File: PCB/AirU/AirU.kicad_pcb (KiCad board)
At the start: 2 copper layers, 11 parts, among them IC1 LD1086DT50TR, IC2 L70B-M39, IC3 NCV21872DR2G, J1 MEM2051-00-195-00-A, J2 ZX62-B-5PA_33_, J3 53261-7008, Q1 MMBT3904, Q2 MMBT3904, U1 ESP32-S3-WROOM-1, U2 CH340E

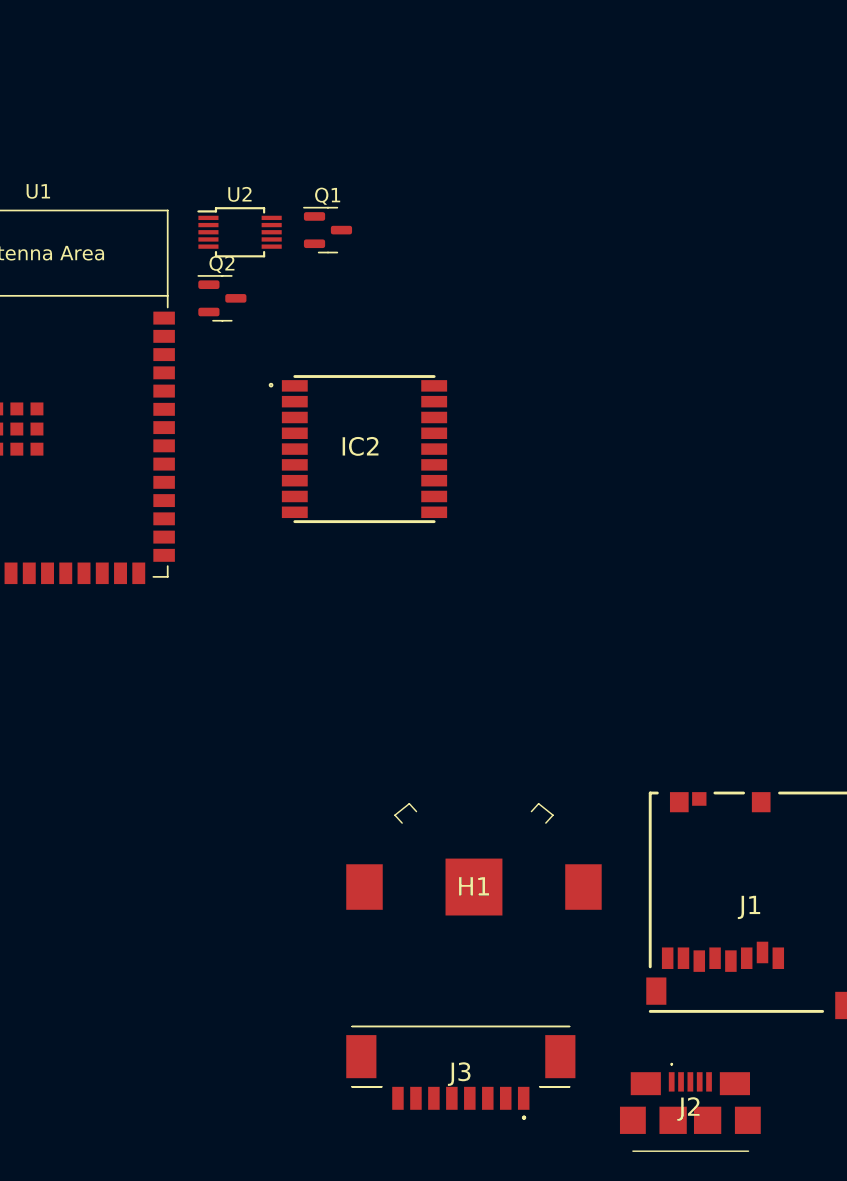
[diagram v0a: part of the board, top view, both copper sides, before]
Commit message: usb to serial done on schematic
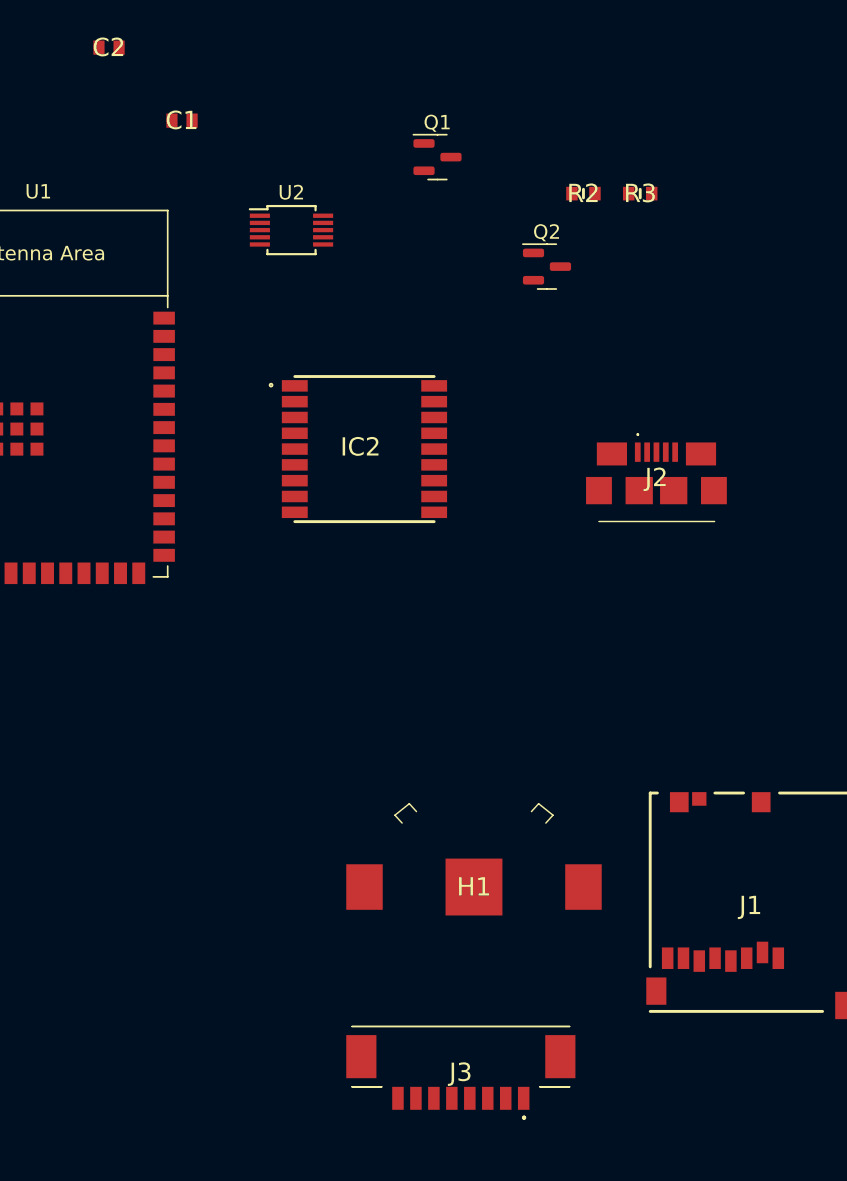
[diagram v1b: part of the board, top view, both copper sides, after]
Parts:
- added C1: 100n, 0603YC104J4T4A:CAPC1608X90N, F.Cu at (78.7, 35.6)
- added C2: 0603YC104J4T4A, 0603YC104J4T4A:CAPC1608X90N, F.Cu at (73.7, 30.5)
- added R2: RC0603FR-0710KL, RC0603FR-0710KL:RESC1608X55N, F.Cu at (106.7, 40.6)
- added R3: RC0603FR-0710KL, RC0603FR-0710KL:RESC1608X55N, F.Cu at (110.6, 40.6)
- moved J2 43.9 mm to (111.8, 61.0)
- moved Q2 22.7 mm to (104.1, 45.7)
- moved Q1 9.16 mm to (96.5, 38.1)
- moved U2 3.58 mm to (86.4, 43.2)
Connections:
- Q1 pad 1: unconnected-(Q1-Pad1) -> Net-(Q1-Pad1)
- Q1 pad 2: unconnected-(Q1-Pad2) -> Net-(Q1-Pad2)
- Q2 pad 1: unconnected-(Q2-Pad1) -> Net-(Q2-Pad1)
- Q2 pad 2: unconnected-(Q2-Pad2) -> Net-(Q2-Pad2)
- U2 pad 4: unconnected-(U2-Pad4) -> GND
- U2 pad 5: unconnected-(U2-Pad5) -> GND
- U2 pad 8: unconnected-(U2-Pad8) -> /U0RXD
- U2 pad 9: unconnected-(U2-Pad9) -> /U0TXD

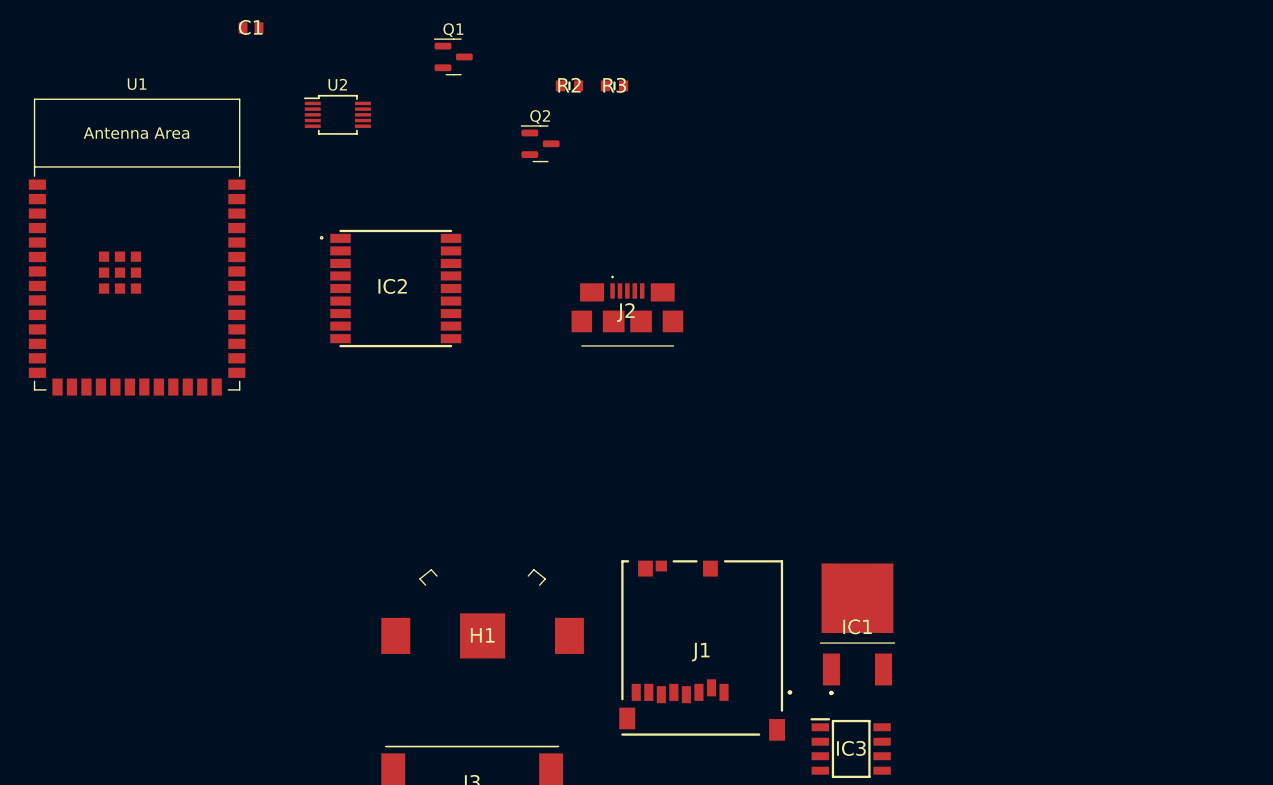
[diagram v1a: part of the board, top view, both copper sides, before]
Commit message: added footprint for lora breakout board
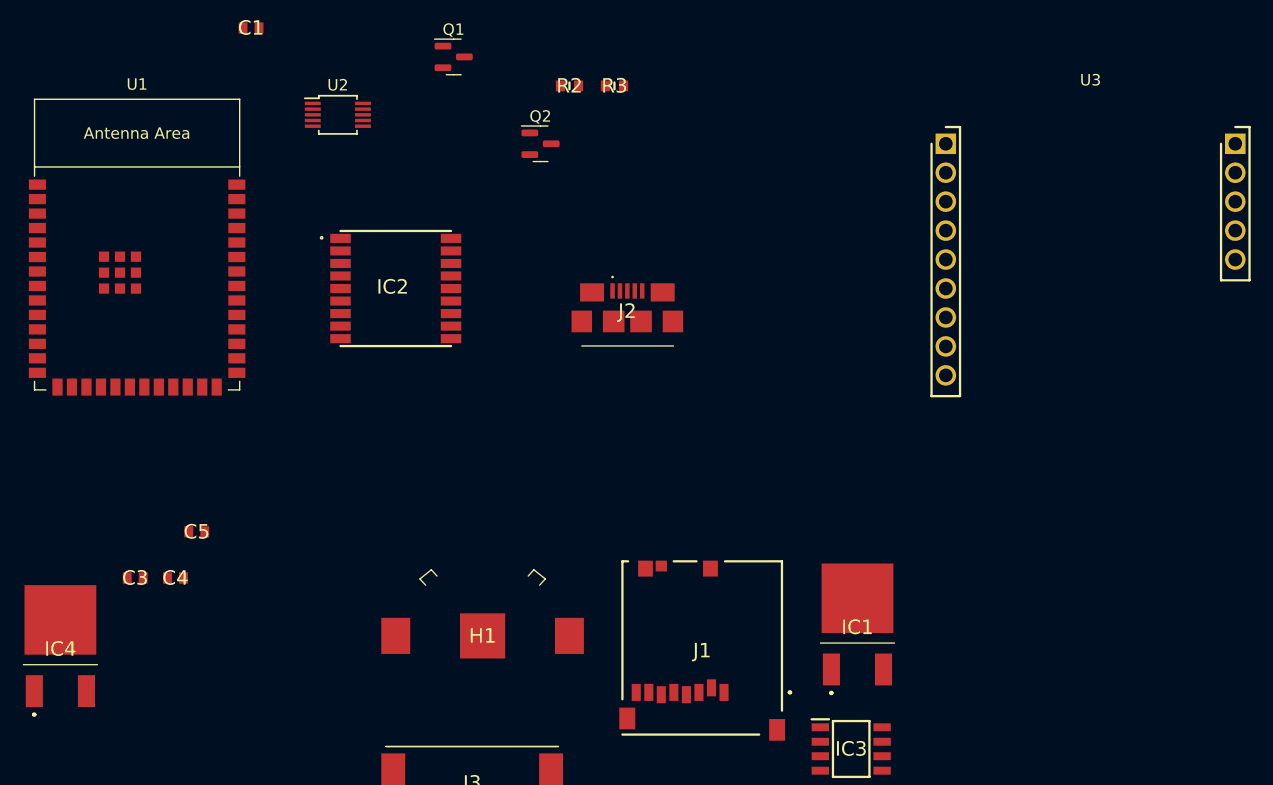
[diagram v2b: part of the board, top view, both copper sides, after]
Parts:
- added C3: 1u, 0603YC105KAT2A:CAPC1608X94N, F.Cu at (68.6, 83.8)
- added C4: 10u, 0603ZDD106KAT2A:CAPC1608X90N, F.Cu at (72.1, 83.8)
- added C5: 10u, 0603ZDD106KAT2A:CAPC1608X90N, F.Cu at (74.0, 79.8)
- added IC4: LD1086DT50TR, LD1086DT50TR:LD1086DT33TR, F.Cu at (62.0, 84.4)
- added U3: LoRa_Breakout, custom_components:LoRa_Breakout, F.Cu at (152.4, 40.6)
- C1: value 100n -> 0.1u
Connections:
- J2 pad 1: unconnected-(J2-Pad1) -> VCC
- J2 pad 2: unconnected-(J2-Pad2) -> /D-
- J2 pad 3: unconnected-(J2-Pad3) -> /D+
- J2 pad 5: unconnected-(J2-Pad5) -> GND
- J2 pad MP1: unconnected-(J2-PadMP1) -> GND
- J2 pad MP2: unconnected-(J2-PadMP2) -> GND
- J2 pad MP3: unconnected-(J2-PadMP3) -> GND
- J2 pad MP4: unconnected-(J2-PadMP4) -> GND
- J2 pad MP5: unconnected-(J2-PadMP5) -> GND
- J2 pad MP6: unconnected-(J2-PadMP6) -> GND
- U1 pad 3: /EN -> VDD

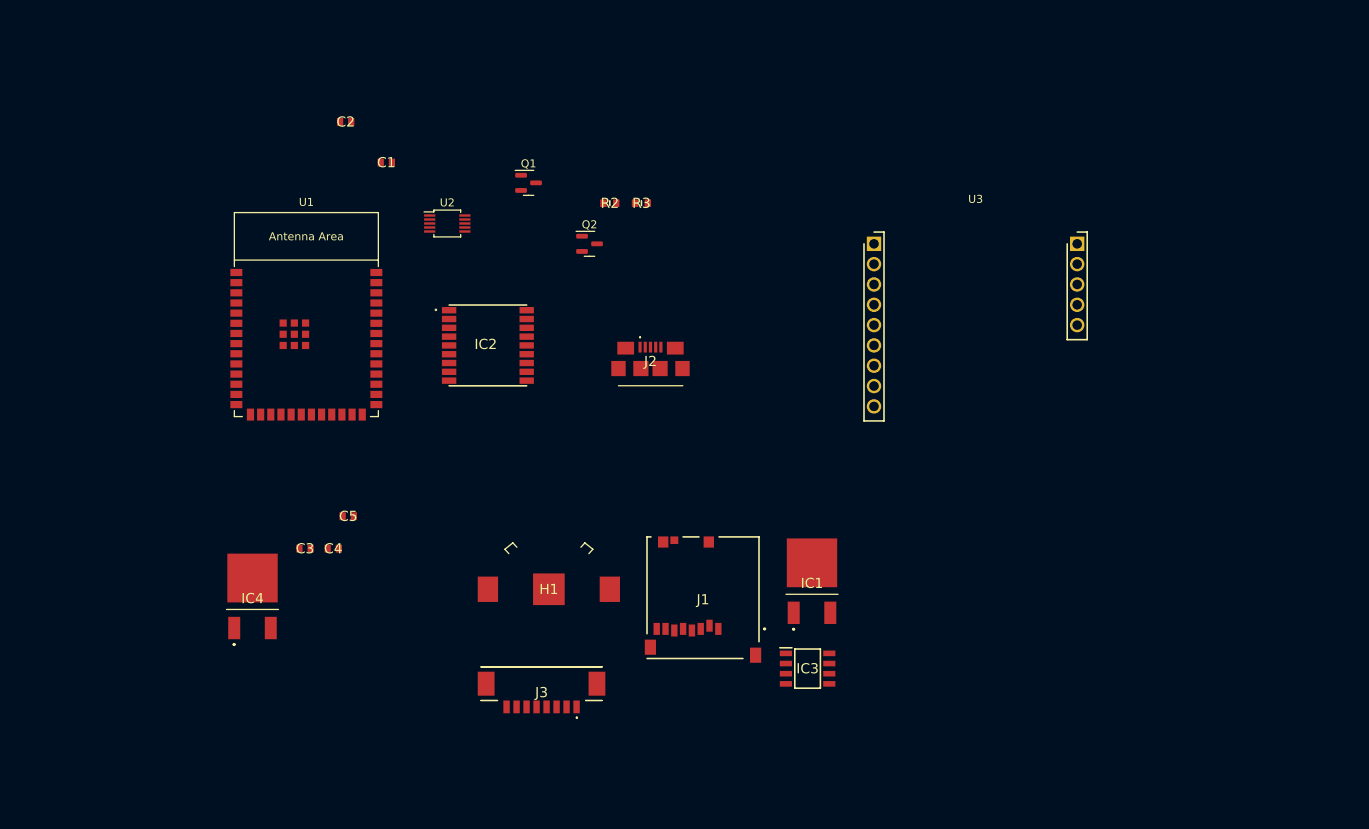
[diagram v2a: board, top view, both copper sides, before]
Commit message: added most parts to pcb
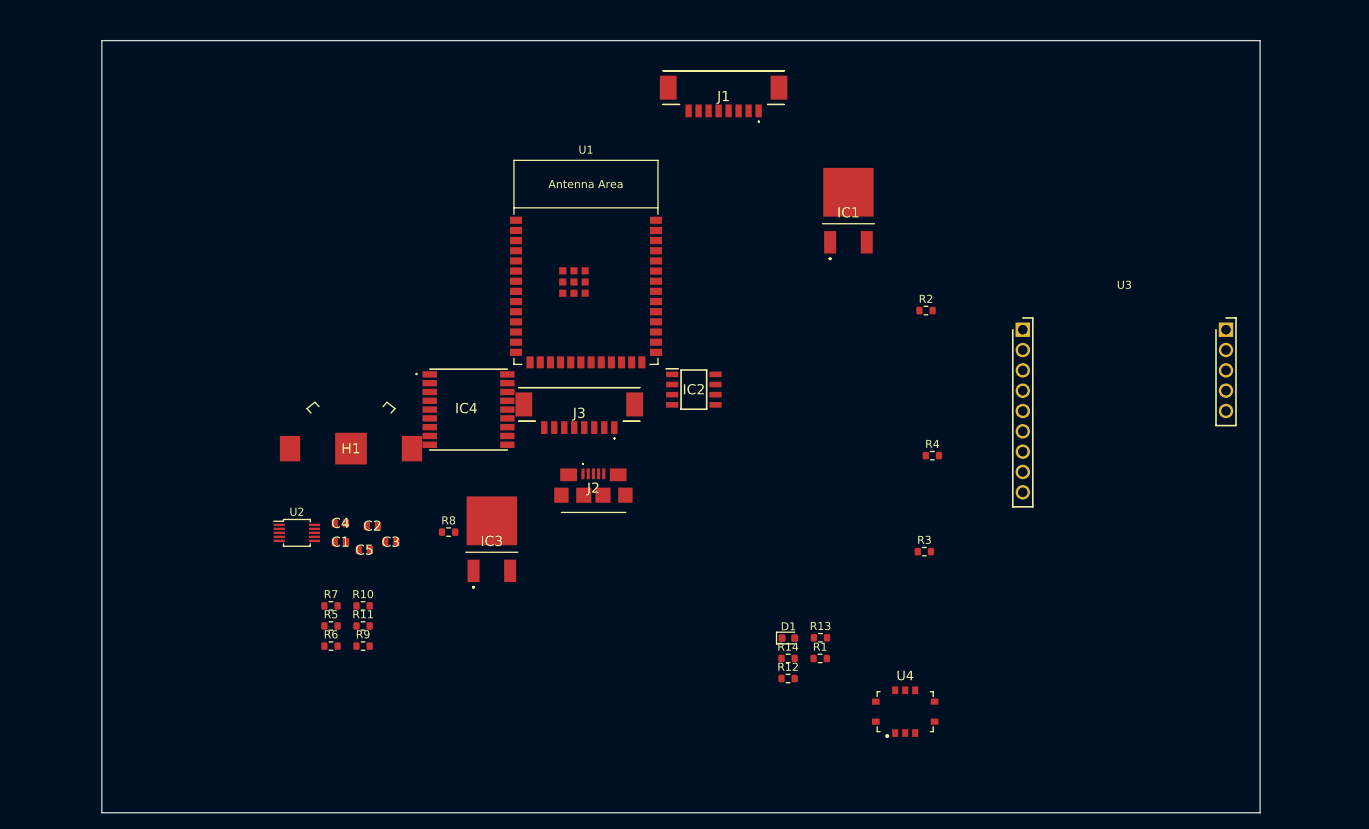
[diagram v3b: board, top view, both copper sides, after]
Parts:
- removed Q1, Q2: MMBT3904, Package_TO_SOT_SMD:SOT-23
- added D1: LED, LED_SMD:LED_0603_1608Metric, F.Cu at (129.0, 95.0)
- added R1: 0, Resistor_SMD:R_0603_1608Metric, F.Cu at (133.0, 97.5)
- added R10: 0, Resistor_SMD:R_0603_1608Metric, F.Cu at (75.8, 91.0)
- added R11: 0, Resistor_SMD:R_0603_1608Metric, F.Cu at (75.8, 93.5)
- added R12: 820, Resistor_SMD:R_0603_1608Metric, F.Cu at (129.0, 100.1)
- added R13: 130, Resistor_SMD:R_0603_1608Metric, F.Cu at (133.0, 95.0)
- added R14: 27, Resistor_SMD:R_0603_1608Metric, F.Cu at (129.0, 97.5)
- added R4: 0, Resistor_SMD:R_0603_1608Metric, F.Cu at (147.0, 72.2)
- added R5: 0, Resistor_SMD:R_0603_1608Metric, F.Cu at (71.8, 93.5)
- added R6: 0, Resistor_SMD:R_0603_1608Metric, F.Cu at (71.8, 96.0)
- added R7: 0, Resistor_SMD:R_0603_1608Metric, F.Cu at (71.8, 91.0)
- added R8: 0, Resistor_SMD:R_0603_1608Metric, F.Cu at (86.5, 81.8)
- added R9: 0, Resistor_SMD:R_0603_1608Metric, F.Cu at (75.8, 96.0)
- added U4: MICS6814, chem_air_u_footprints:PLCC125P750X550X150-16N, F.Cu at (143.6, 104.2)
- C1: value 0.1u -> 0603YC105KAT2A; footprint 0603YC104J4T4A:CAPC1608X90N -> 0603YC105KAT2A:CAPC1608X94N
- C2: value 0603YC104J4T4A -> 10u; footprint 0603YC104J4T4A:CAPC1608X90N -> 0603ZDD106KAT2A:CAPC1608X90N
- C3: value 1u -> 0603YC104J4T4A; footprint 0603YC105KAT2A:CAPC1608X94N -> 0603YC104J4T4A:CAPC1608X90N
- C5: value 10u -> 0.1u; footprint 0603ZDD106KAT2A:CAPC1608X90N -> 0603YC104J4T4A:CAPC1608X90N
- IC2: value L70B-M39 -> NCV21872DR2G; footprint L70B-M39:L76 -> NCV21872DR2G:SOIC127P600X175-8N
- IC3: value NCV21872DR2G -> LD1086DT50TR; footprint NCV21872DR2G:SOIC127P600X175-8N -> LD1086DT50TR:LD1086DT33TR
- IC4: value LD1086DT50TR -> L70B-M39; footprint LD1086DT50TR:LD1086DT33TR -> L70B-M39:L76
- J1: value MEM2051-00-195-00-A -> 53261-7008; footprint MEM2051-00-195-00-A:MEM20510019500A -> 53261-7008:532617008
- R2, R3: value RC0603FR-0710KL -> 0; footprint RC0603FR-0710KL:RESC1608X55N -> Resistor_SMD:R_0603_1608Metric
- moved J1 64.0 mm to (120.9, 26.2)
- moved R3 56.1 mm to (146.0, 84.2)
- moved C2 50.6 mm to (77.0, 81.0)
- moved C1 47.8 mm to (73.0, 83.0)
- moved IC1 46.5 mm to (136.5, 36.2)
- moved IC3 45.0 mm to (91.9, 77.3)
- moved U2 43.0 mm to (67.6, 81.8)
- moved R2 41.7 mm to (146.2, 54.1)
- moved U1 35.6 mm to (103.7, 51.0)
- moved J3 35.2 mm to (102.9, 65.8)
- moved IC4 32.5 mm to (89.0, 66.4)
- moved H1 30.3 mm to (74.3, 71.3)
- moved IC2 26.3 mm to (117.2, 63.9)
- moved U3 21.5 mm to (171.0, 51.4)
- moved J2 17.4 mm to (104.6, 76.8)
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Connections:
- C1 pad 1: VDD -> GND
- C1 pad 2: GND -> VDD
- C2 pad 1: unconnected-(C2-Pad1) -> GND
- C2 pad 2: unconnected-(C2-Pad2) -> VCC
- C3 pad 1: GND -> unconnected-(C3-Pad1)
- C3 pad 2: VDD -> unconnected-(C3-Pad2)
- C4 pad 2: VCC -> VDD
- C5 pad 1: GND -> VDD
- C5 pad 2: VDD -> GND
- IC3 pad 1: unconnected-(IC3-Pad1) -> GND
- IC3 pad 2: unconnected-(IC3-Pad2) -> VDD
- IC3 pad 3: unconnected-(IC3-Pad3) -> VCC
- IC4 pad 1: GND -> unconnected-(IC4-Pad1)
- IC4 pad 2: VDD -> unconnected-(IC4-Pad2)
- IC4 pad 3: VCC -> unconnected-(IC4-Pad3)
- J1 pad MP1: unconnected-(J1-PadMP1) -> GND
- J1 pad MP2: unconnected-(J1-PadMP2) -> GND
- R2 pad 1: Net-(Q2-Pad2) -> /LORA_SCLK
- R2 pad 2: Net-(Q1-Pad1) -> /GPIO14
- R3 pad 1: Net-(Q1-Pad2) -> /LORA_MISO
- R3 pad 2: Net-(Q2-Pad1) -> /GPIO13
- U1 pad 12: /GPIO8 -> /CO_VALUE
- U2 pad 6: unconnected-(U2-Pad6) -> Net-(D1-Pad2)
- U3 pad 1: unconnected-(U3-Pad1) -> VDD
- U3 pad 10: unconnected-(U3-Pad10) -> /LORA_DIO1
- U3 pad 11: unconnected-(U3-Pad11) -> /LORA_DIO2
- U3 pad 12: unconnected-(U3-Pad12) -> /LORA_DIO3
- U3 pad 13: unconnected-(U3-Pad13) -> /LORA_DIO4
- U3 pad 14: unconnected-(U3-Pad14) -> /LORA_DIO5
- U3 pad 2: unconnected-(U3-Pad2) -> GND
- U3 pad 3: unconnected-(U3-Pad3) -> VDD
- U3 pad 4: unconnected-(U3-Pad4) -> /LORA_DIO0
- U3 pad 5: unconnected-(U3-Pad5) -> /LORA_SCLK
- U3 pad 6: unconnected-(U3-Pad6) -> /LORA_MISO
- U3 pad 7: unconnected-(U3-Pad7) -> /LORA_MOSI
- U3 pad 8: unconnected-(U3-Pad8) -> /LORA_NSS
- U3 pad 9: unconnected-(U3-Pad9) -> /LORA_RST
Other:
- board outline added: 144.8 x 96.5 mm

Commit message: schematic complete
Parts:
- removed C3: 0603YC104J4T4A, 0603YC104J4T4A:CAPC1608X90N
- removed H1: 2894, 2984:2894
- removed IC1: LD1086DT50TR, LD1086DT50TR:LD1086DT33TR
- removed IC2: NCV21872DR2G, NCV21872DR2G:SOIC127P600X175-8N
- removed IC4: L70B-M39, L70B-M39:L76
- removed J3: 53261-7008, 53261-7008:532617008
- added R15: 3k, Resistor_SMD:R_0603_1608Metric, F.Cu at (153.3, 45.6)
- added R16: 3k, Resistor_SMD:R_0603_1608Metric, F.Cu at (145.2, 50.6)
- added R17: 10k, Resistor_SMD:R_0603_1608Metric, F.Cu at (109.6, 82.5)
- added R18: 10k, Resistor_SMD:R_0603_1608Metric, F.Cu at (105.6, 81.8)
- added U5: HDC2010YPAR, footprints:HDC2010YPAR, F.Cu at (148.7, 53.2)
- C1: value 0603YC105KAT2A -> 0.1u
- moved R7 89.7 mm to (149.2, 45.6)
- moved R11 82.9 mm to (145.2, 48.1)
- moved C2 78.2 mm to (149.0, 50.6)
- moved U3 73.1 mm to (98.2, 45.1)
- moved C4 72.6 mm to (142.8, 60.4)
- moved U2 72.6 mm to (137.3, 61.5)
- moved R8 65.3 mm to (145.2, 53.2)
- moved C1 64.9 mm to (135.4, 65.1)
- moved J1 57.8 mm to (93.0, 76.8)
- moved IC3 56.0 mm to (138.4, 46.2)
- moved R12 55.7 mm to (149.2, 48.1)
- moved R14 54.4 mm to (145.2, 45.6)
- moved R2 50.7 mm to (105.6, 84.3)
- moved R3 48.5 mm to (97.5, 83.9)
- moved R4 46.9 mm to (101.5, 83.9)
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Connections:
- J1 pad 1: unconnected-(J1-Pad1) -> VCC
- J1 pad 2: unconnected-(J1-Pad2) -> GND
- J1 pad 3: unconnected-(J1-Pad3) -> /GPIO45
- J1 pad 5: unconnected-(J1-Pad5) -> /GPIO48
- J1 pad 6: unconnected-(J1-Pad6) -> /GPIO46
- U1 pad 12: /CO_VALUE -> /GPIO8
- U4 pad 8: /CO_VALUE -> /GPIO18

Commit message: part of layout done
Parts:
- moved R10 100.0 mm to (183.9, 50.9), turned to -90 degrees
- moved U3 90.6 mm to (184.9, 18.8)
- moved R5 83.2 mm to (166.1, 43.1), turned to 180 degrees
- moved R3 82.9 mm to (166.1, 37.3), turned to 180 degrees
- moved R2 78.5 mm to (166.1, 34.4), turned to 180 degrees
- moved R4 77.9 mm to (166.1, 40.2), turned to 180 degrees
- moved J1 77.6 mm to (150.7, 24.9)
- moved R9 75.6 mm to (181.0, 50.9), turned to -90 degrees
- moved C5 74.6 mm to (167.1, 26.9), turned to 90 degrees
- moved R1 73.2 mm to (166.1, 31.5), turned to 180 degrees
- moved R6 68.7 mm to (166.1, 46.0), turned to 180 degrees
- moved R18 66.4 mm to (152.6, 34.9), turned to 90 degrees
- moved IC3 64.2 mm to (74.3, 44.0)
- moved R17 61.7 mm to (148.8, 34.9), turned to 90 degrees
- moved J2 52.7 mm to (128.0, 25.3), turned to 180 degrees
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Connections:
- R9 pad 2: /GPIO14 -> /GPIO16
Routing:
- net GND: track 0.00 -> 73.9 mm
- net VDD: track 0.00 -> 62.9 mm
- net /LORA_DIO1: track 0.00 -> 35.5 mm
- net /LORA_DIO2: track 0.00 -> 31.8 mm
- net /LORA_DIO3: track 0.00 -> 28.0 mm
- net /GPIO4: track 0.00 -> 26.2 mm
- net /LORA_DIO4: track 0.00 -> 24.3 mm
- net /GPIO6: track 0.00 -> 22.2 mm
- net /LORA_DIO5: track 0.00 -> 20.6 mm
- net /GPIO15: track 0.00 -> 14.8 mm
- net /GPIO7: track 0.00 -> 14.2 mm
- net VCC: track 0.00 -> 7.71 mm
- net /GPIO45: track 0.00 -> 6.29 mm
- net /GPIO46: track 0.00 -> 6.29 mm
- net /LORA_RST: track 0.00 -> 6.05 mm
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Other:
- board size 144.8 x 96.5 mm -> 167 x 87.9 mm
